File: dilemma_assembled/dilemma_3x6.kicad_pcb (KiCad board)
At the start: 2 copper layers, 153.1 x 110.3 mm, 129 parts, among them J1 USB_C_Receptacle_USB2.0, J102 Serial, J103 Serial, J105 Conn_01x04_Female, J107 Conn_01x08_Female, J108 Conn_01x01_Female, J109 Conn_01x01_Female, J113 Cirque, J5 Conn_01x02, SW1 SW_Push, SW101 SW_Push, SW102 SW_Push, SW103 SW_Push, SW104 SW_Push, SW105 SW_Push, SW106 SW_Push, SW107 SW_Push, SW108 SW_Push, SW109 SW_Push, SW110 SW_SPST, SW111 SW_SPST, SW112 SW_Push, SW113 SW_Push, SW114 SW_Push, SW115 SW_Push, SW116 SW_Push, SW117 SW_Push, SW118 SW_Push, SW119 locked, SW120 SW_Push, SW121 SW_Push, SW122 SW_Push, SW2 SW_Push, U1 RP2040, U2 GD25Q80CEIGR, U3 XC6210B332MR-G, Y1 Crystal_GND24

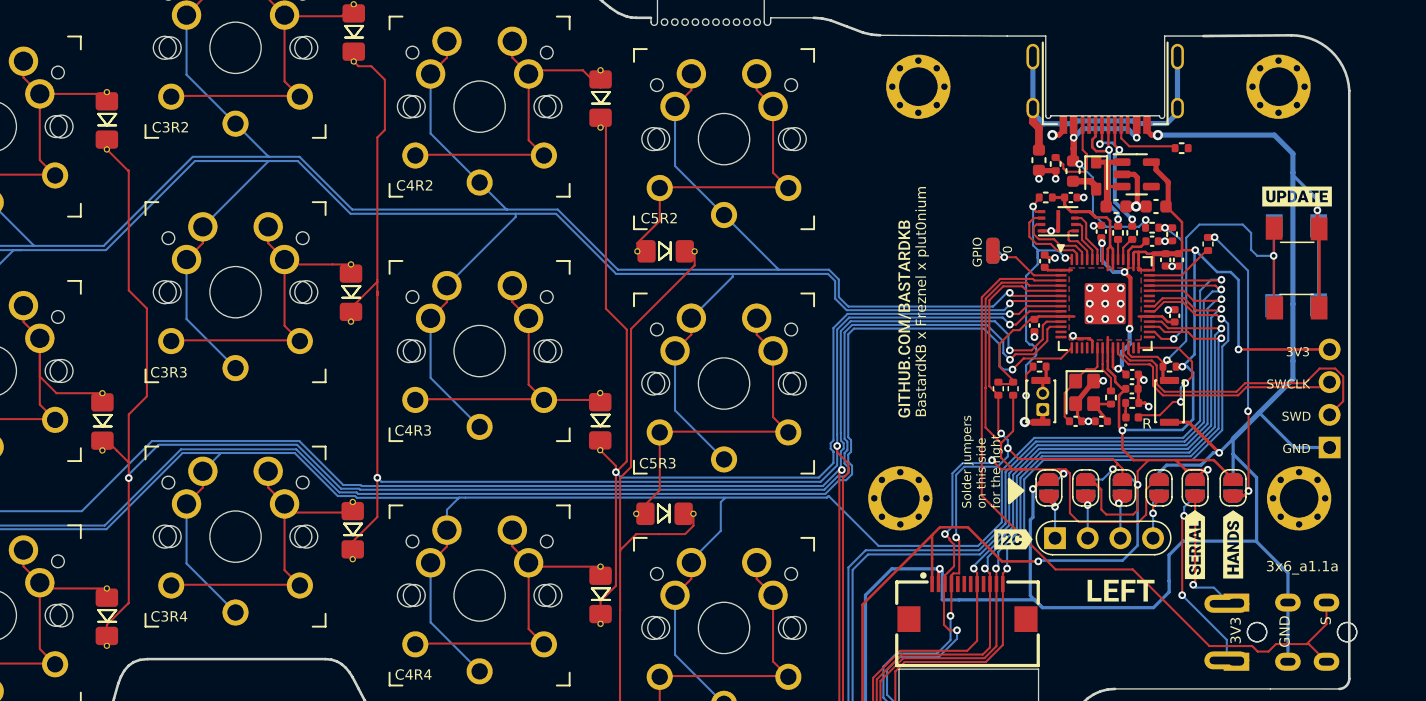
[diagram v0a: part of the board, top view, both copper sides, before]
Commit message: add back puck
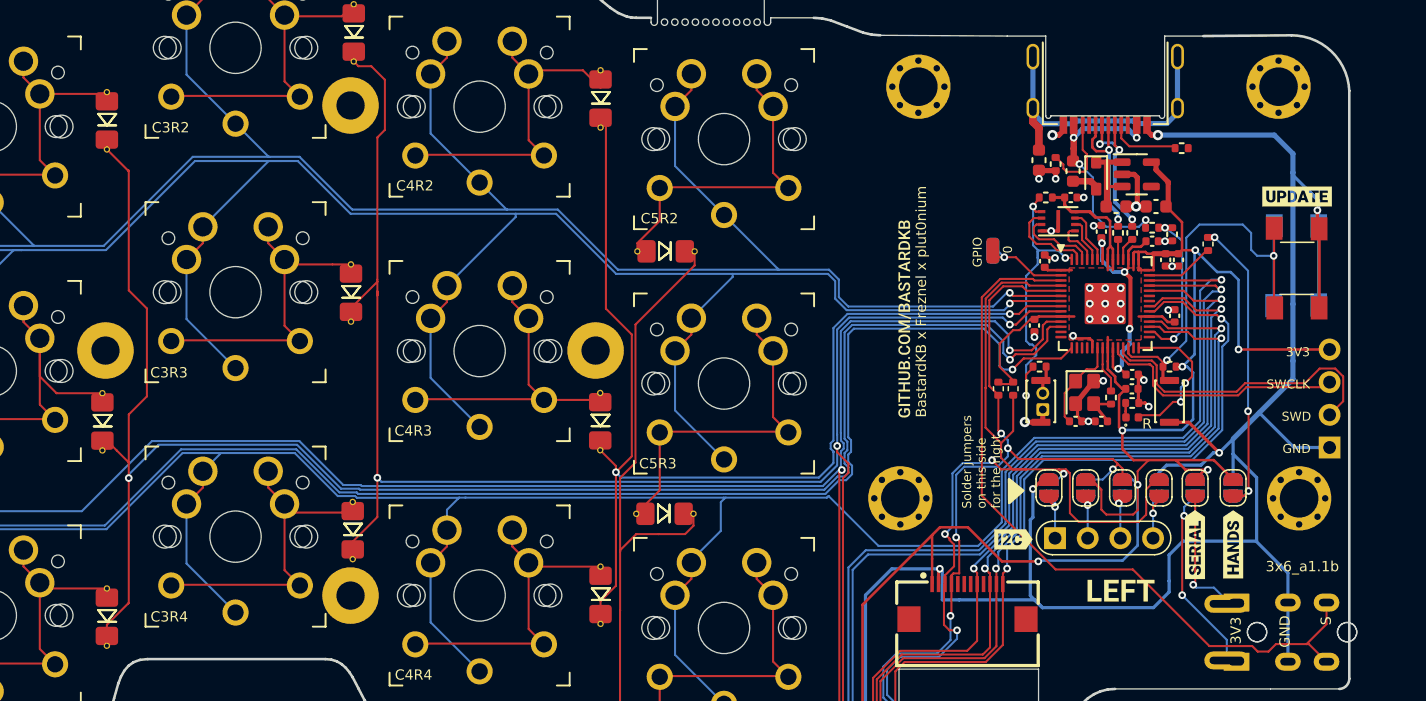
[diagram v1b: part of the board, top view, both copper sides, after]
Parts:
- added H111: t, local-libraries:Tenting_Puck, F.Cu at (100.4, 59.2)
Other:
- board text added: "3x6_a1.1b"
- board text removed: "3x6_a1.1a"

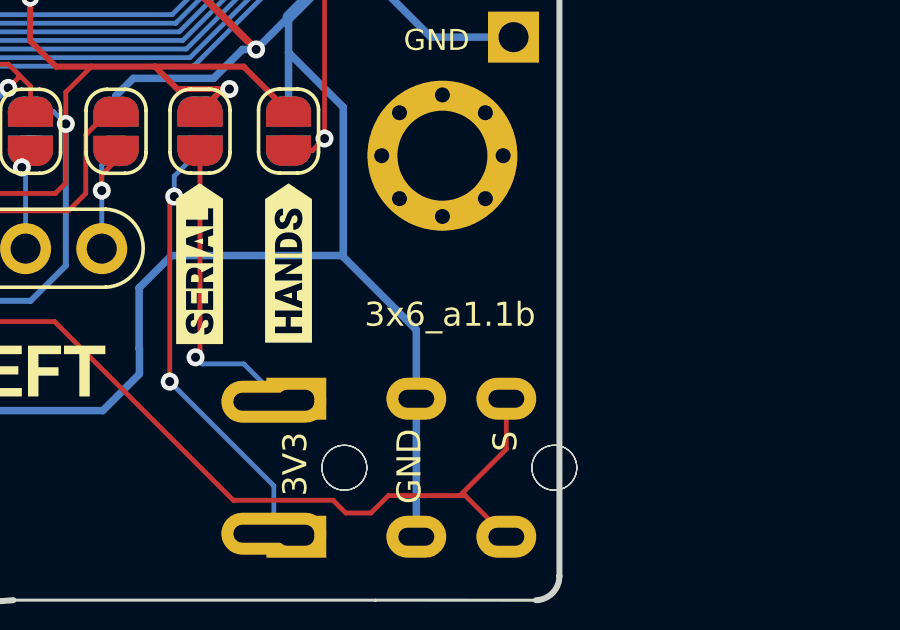
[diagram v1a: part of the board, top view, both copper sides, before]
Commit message: fix R103 R104 bom
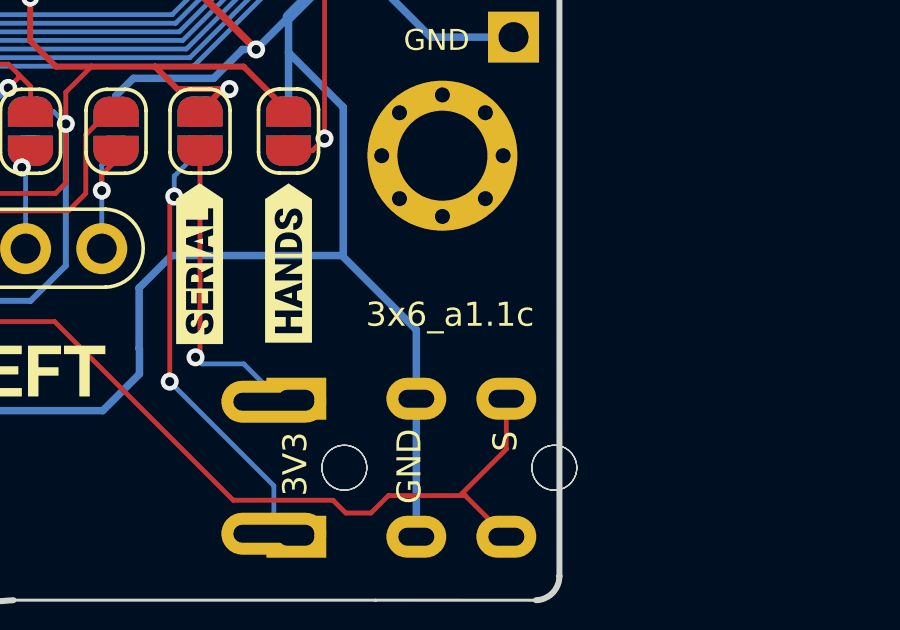
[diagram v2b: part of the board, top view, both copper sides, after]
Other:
- board text added: "3x6_a1.1c"
- board text removed: "3x6_a1.1b"
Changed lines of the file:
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@@
     (effects (font (size 0.7 0.7) (thickness 0.12)))
   )
-  (gr_text "3x6_a1.1b" (at 174.382352 75.97) (layer "F.SilkS")
+  (gr_text "3x6_a1.1c" (at 174.382352 75.97) (layer "F.SilkS")
     (effects (font (size 0.8 0.8) (thickness 0.12)))
   )
